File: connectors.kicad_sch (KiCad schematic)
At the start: 10 parts, among them CN102 EXPANSION, CN105 JOY1, CN202 HuCARD

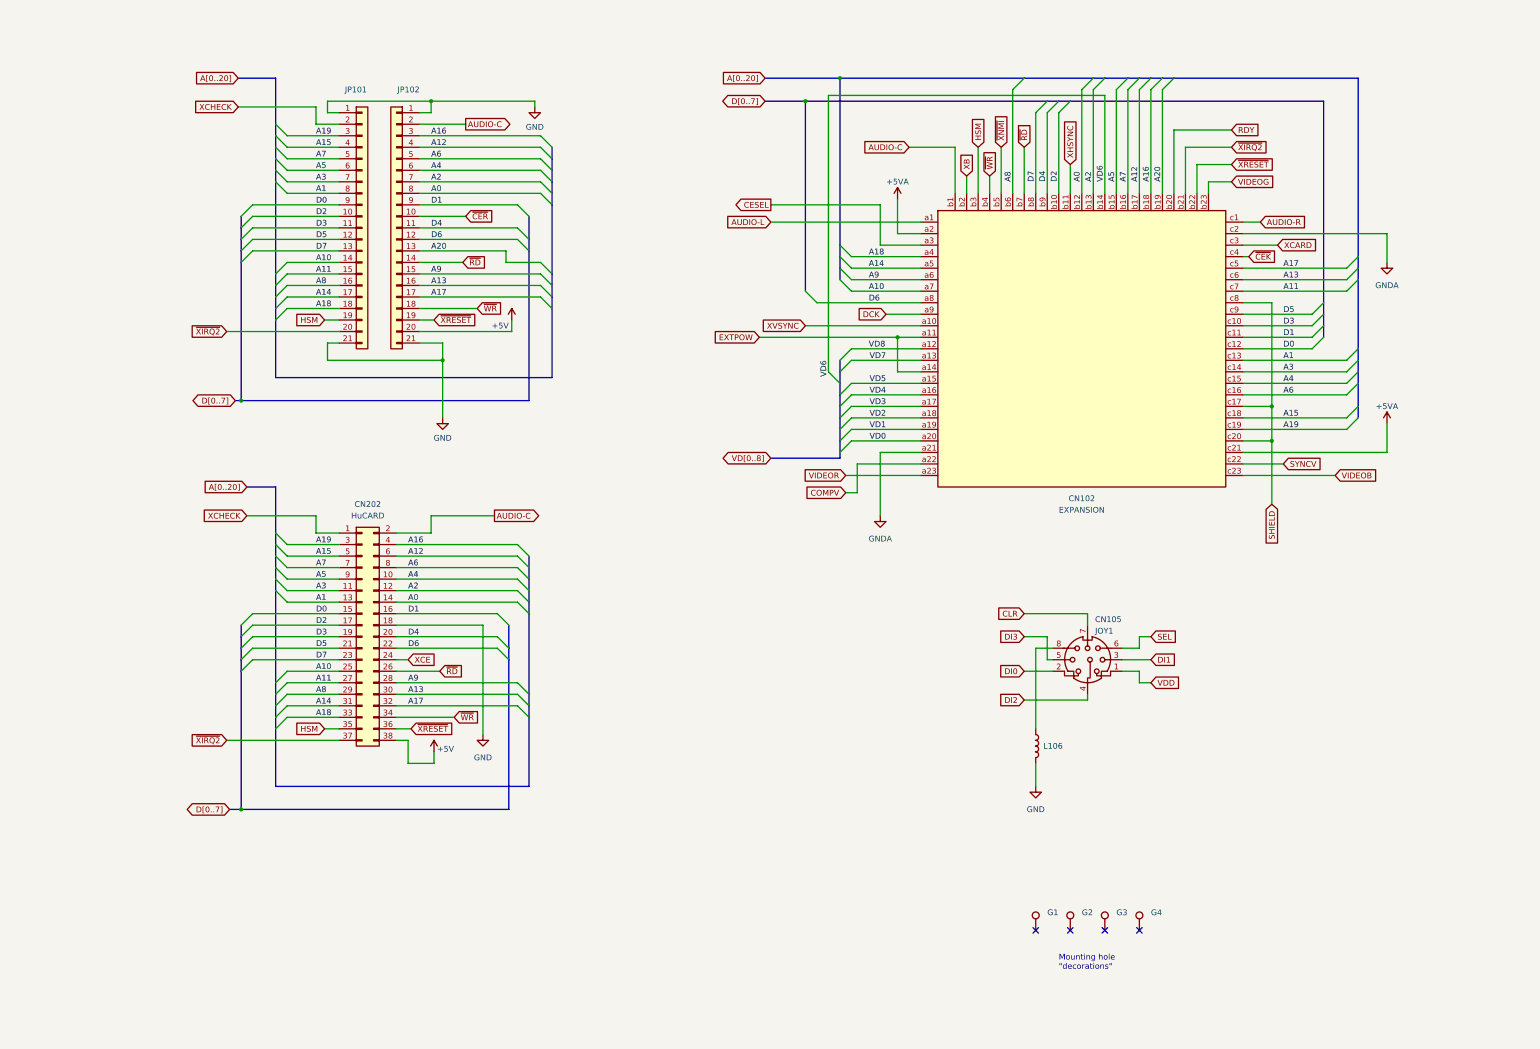
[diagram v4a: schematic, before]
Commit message: Silkscreen stuff, tidy schematics, corrections.
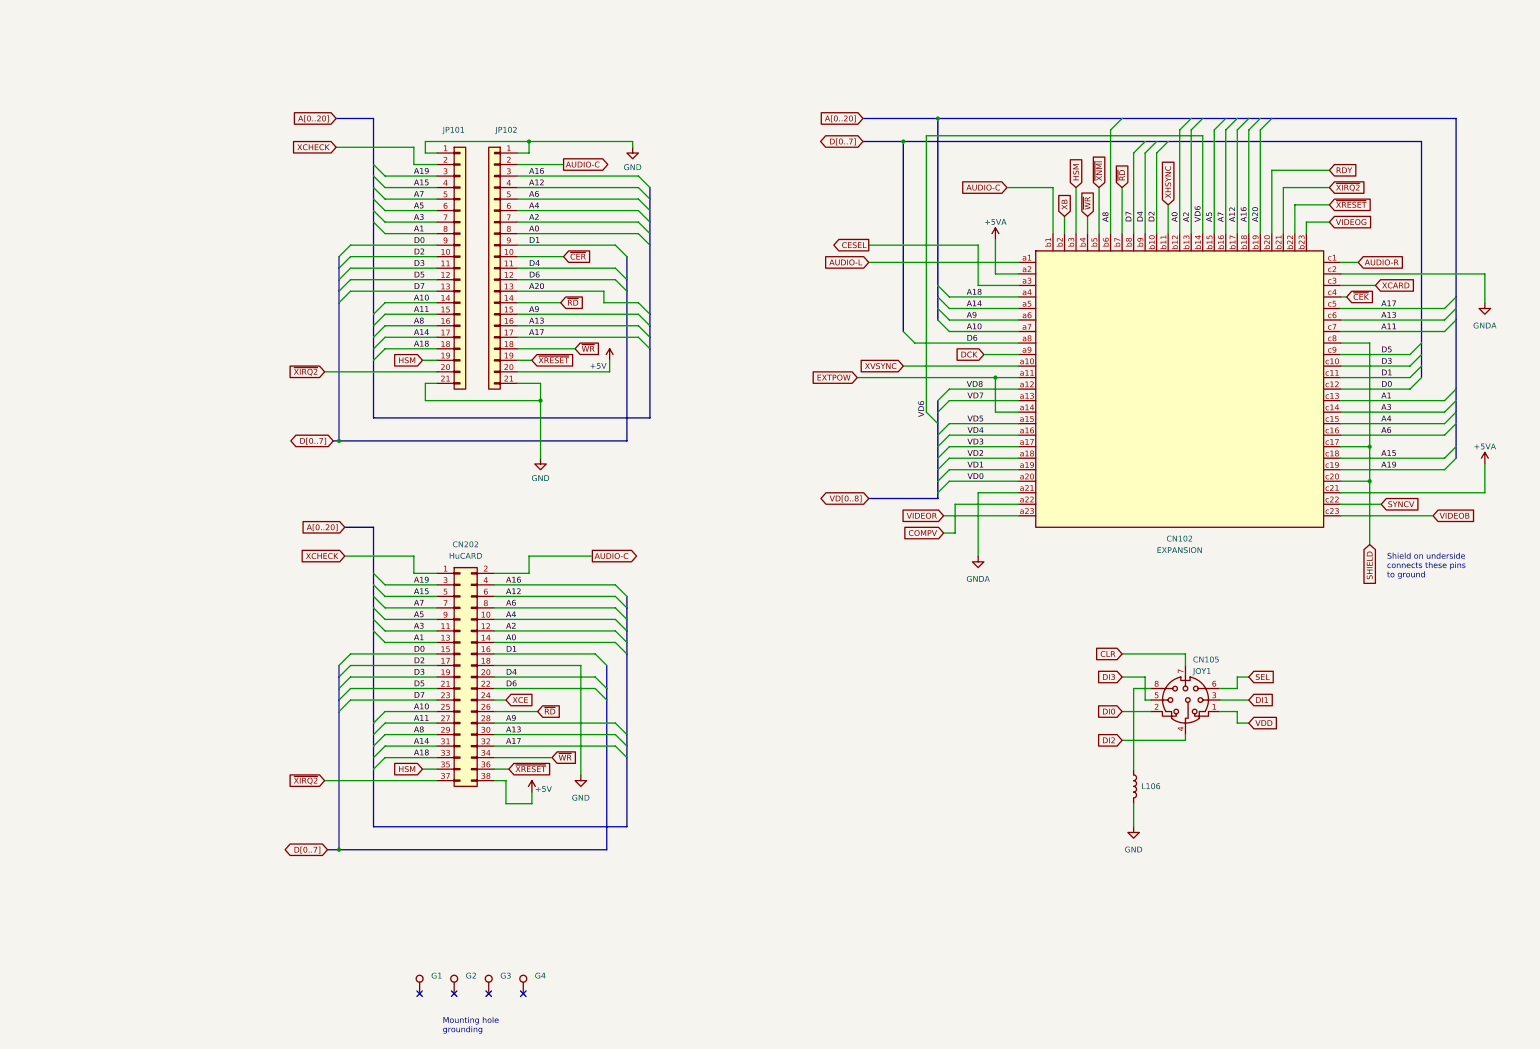
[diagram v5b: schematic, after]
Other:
- note added: "Mounting hole grounding"
- note added: "Shield on underside connects these pins to ground"
- note removed: "Mounting hole "decorations""
- title: (none) -> PC Engine Connectors
- moved on the sheet: CN102, CN105, CN202, G1, G2, G3, G4, JP101, JP102, L106

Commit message: Silkscreen/DRC fixes
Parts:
- L106: footprint A-PCENGINE:L-5.00mm -> A-PCENGINE:L-5.00mm_Small_Silk
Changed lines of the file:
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@@
       (effects (font (size 1.27 1.27)))
     )
-    (property "Footprint" "A-PCENGINE:L-5.00mm" (at 261.62 186.69 0)
+    (property "Footprint" "A-PCENGINE:L-5.00mm_Small_Silk" (at 261.62 186.69 0)
       (effects (font (size 1.27 1.27)) hide)
     )

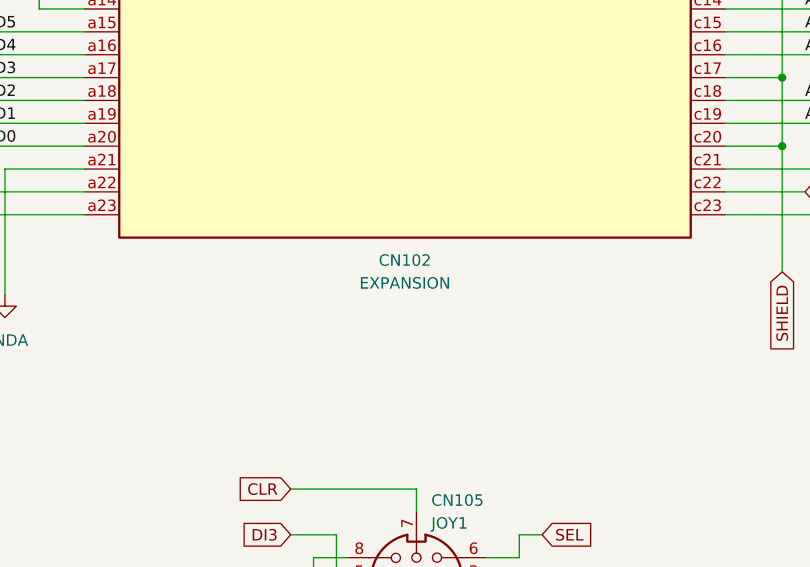
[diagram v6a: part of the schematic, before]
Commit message: Remove some sharp corners on traces, generate BOM.
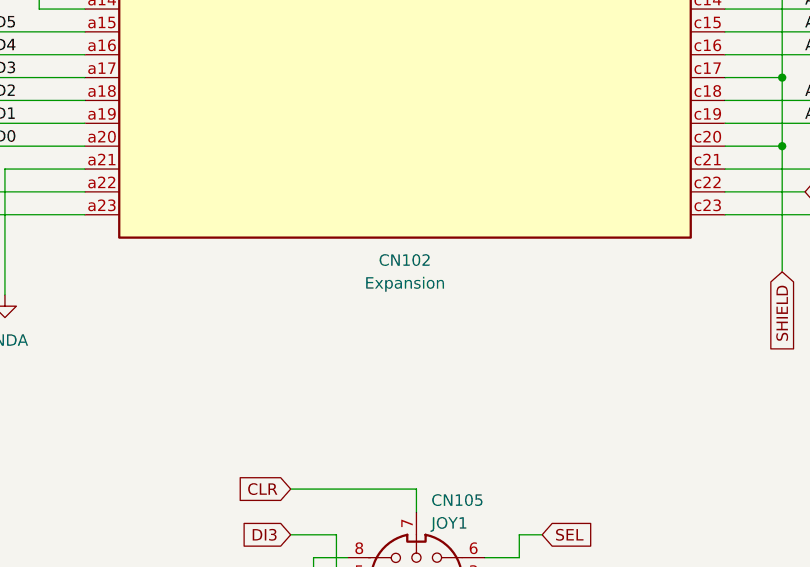
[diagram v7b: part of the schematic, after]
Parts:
- CN102: value EXPANSION -> Expansion
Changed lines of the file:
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@@
       (effects (font (size 1.27 1.27)))
     )
-    (property "Value" "EXPANSION" (at 271.78 134.62 0)
+    (property "Value" "Expansion" (at 271.78 134.62 0)
       (effects (font (size 1.27 1.27)))
     )
